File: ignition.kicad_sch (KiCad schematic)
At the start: 18 parts, among them J2 Centroid, J4 PYRO1, Q1 PMOS-GSD, Q2 Q_NMOS_GSD, Q3 Q_NMOS_GSD, Q4 Q_NMOS_GSD, U4 CPC1135N

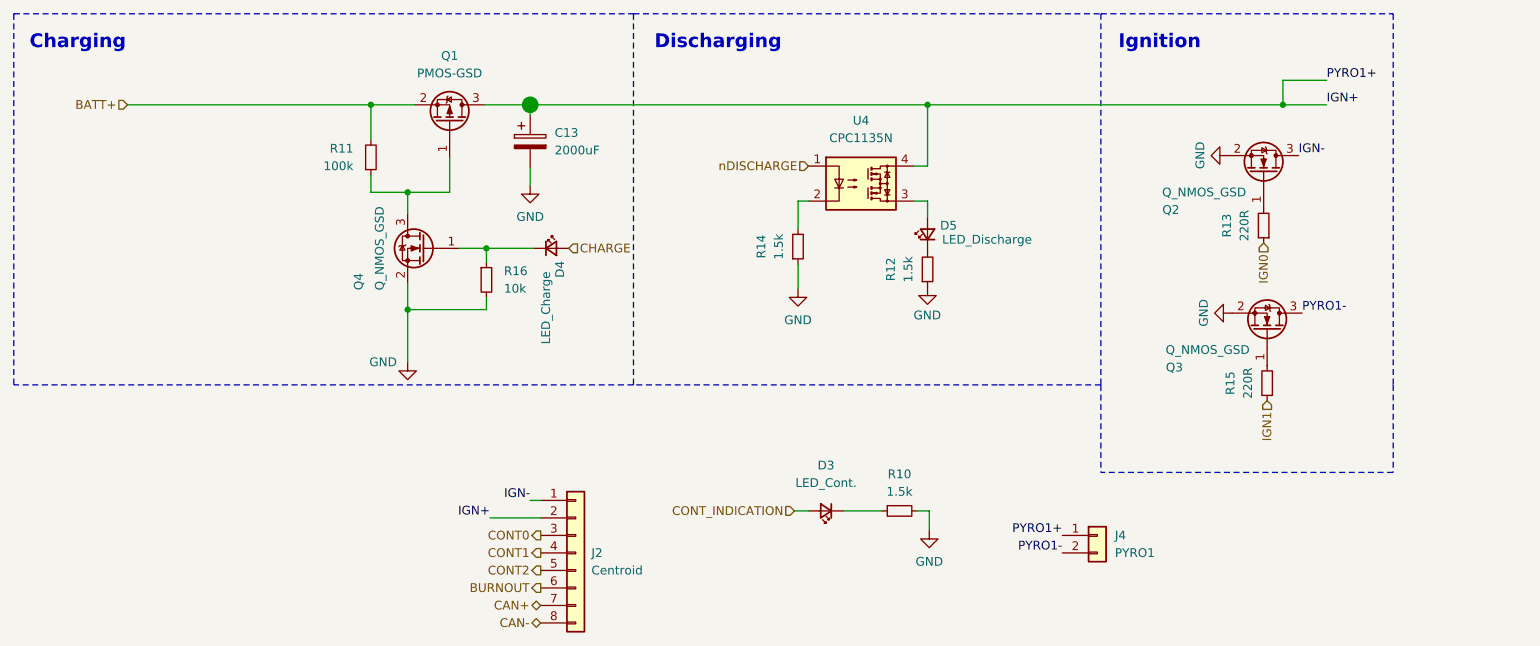
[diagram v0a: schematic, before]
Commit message: #1 Add PYRO2 channel
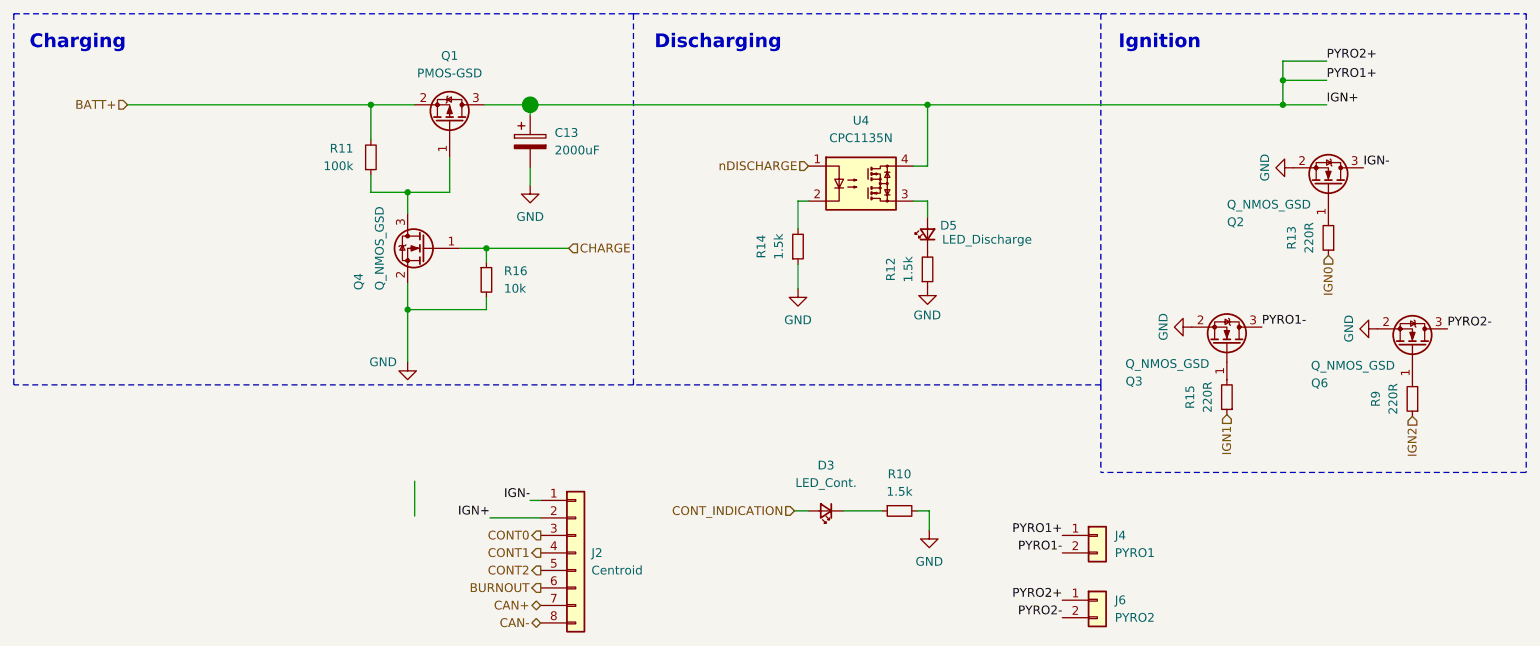
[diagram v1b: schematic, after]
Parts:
- removed D4: LED_Charge, LED_SMD:LED_0603_1608Metric, symbol Device:LED_Small
- added J6: PYRO2, Connector_PinHeader_2.54mm:PinHeader_1x02_P2.54mm_Vertical_SMD_Pin1Left, symbol Connector_Generic:Conn_01x02
- added Q6: Q_NMOS_GSD, Package_TO_SOT_SMD:SOT-23, symbol Device:Q_NMOS_GSD
- added R9: 220R, Resistor_SMD:R_0402_1005Metric, symbol Device:R_Small
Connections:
- net CHARGE: now also Q4.1 (G), R16.1
- net GND: now also Q6.2 (S)
- net IGN+: now also J6.1 (Pin_1)
- new net: Q6.1 (G), R9.2
- new net IGN2: R9.1
- new net PYRO2-: J6.2 (Pin_2), Q6.3 (D)
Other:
- moved on the sheet: Q2, Q3, R13, R15

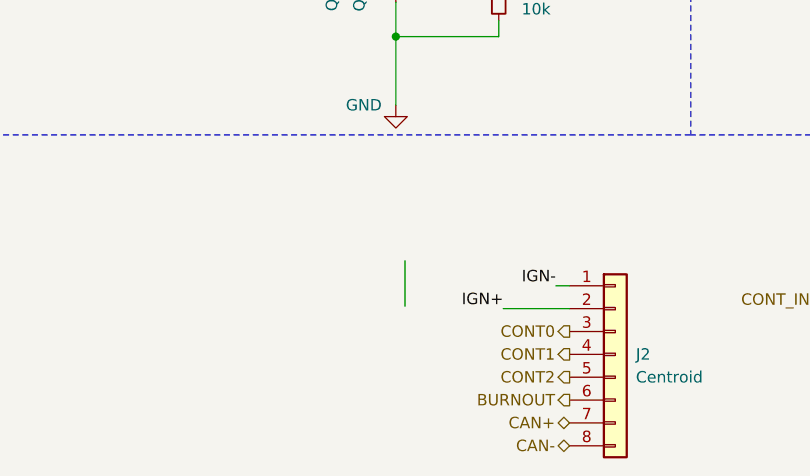
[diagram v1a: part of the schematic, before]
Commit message: #1 Make connections for IGN2
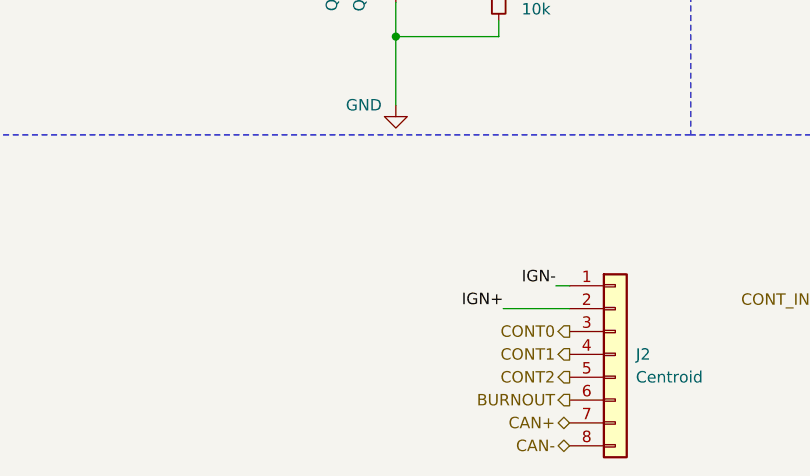
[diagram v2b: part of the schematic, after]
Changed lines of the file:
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@@
-    (stroke (width 0) (type solid) (color 0 0 0 0))
-  )
-  (wire (pts (xy 105.41 107.442) (xy 105.41 112.522))
     (stroke (width 0) (type solid) (color 0 0 0 0))
   )
